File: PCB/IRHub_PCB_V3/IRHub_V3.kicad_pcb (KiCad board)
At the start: 2 copper layers, 85 parts, among them Q1 UMH3N, SW1 SW_Push, U1 DRV2605LDGS

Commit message: power pcb done
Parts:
- 5V1, TP9, T_D+1, T_D-1, T_D6, T_D7, T_GND1, T_RX1, T_TX1: footprint TestPoint:TestPoint_Pad_D2.0mm -> TestPoint:TestPoint_Pad_D1.0mm
- moved TP9 173.7 mm to (174.5, 120.5), turned to 180 degrees
- moved T_GND1 154.7 mm to (154.2, 128.5), turned to 180 degrees
- moved 5V1 154.4 mm to (145.8, 128.5), turned to 180 degrees
- moved T_D-1 151.6 mm to (151.5, 128.5), turned to 180 degrees
- moved T_D+1 151.1 mm to (148.5, 128.5), turned to 180 degrees
- moved AMS1117 147.6 mm to (161.5, 121.2)
- moved D25 146.3 mm to (184.9, 112.1), turned to -109.1 degrees
- moved D26 145.6 mm to (181.7, 118.8), turned to -120.6 degrees
- moved CH340C1 145.4 mm to (150.1, 122.5), turned to 90 degrees
- moved T_RX1 144.9 mm to (160.8, 98.0)
- moved ESP1 144.6 mm to (150.0, 99.5)
- moved C4 144.3 mm to (168.5, 124.8)
- moved D27 143.6 mm to (177.3, 124.8), turned to -132.1 degrees
- moved D1 143.0 mm to (141.5, 136.0), turned to 166.9 degrees
- moved T_TX1 142.8 mm to (160.8, 95.8), turned to 180 degrees
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
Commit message: finished placement
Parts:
- removed ME6211: ME6211C33M5, Package_TO_SOT_SMD:SOT-23-5
- moved R10 158.4 mm to (178.2, 116.1), turned to -22.5 degrees
- moved R9 152.9 mm to (181.3, 91.3), turned to 22.5 degrees
- moved MFT1 152.3 mm to (170.7, 100.7)
- moved R11 147.6 mm to (158.5, 131.2), turned to -67.5 degrees
- moved BZR1 141.6 mm to (178.4, 100.8), turned to -90 degrees
- moved R16 137.3 mm to (162.3, 108.8)
- moved R15 136.2 mm to (162.2, 103.2), turned to 180 degrees
- moved R12 135.6 mm to (133.9, 128.2), turned to -112.5 degrees
- moved R8 133.6 mm to (166.1, 71.8), turned to 67.5 degrees
- moved R18 132.9 mm to (162.3, 106.0)
- moved R5 132.7 mm to (134.2, 118.0), turned to -90 degrees
- moved MFT2 122.3 mm to (130.1, 118.0), turned to 180 degrees
- moved R6 122.1 mm to (137.7, 100.0)
- moved DispTouch1 120.0 mm to (169.4, 81.8), turned to 90 degrees
- moved LRA1 118.6 mm to (130.5, 92.0), turned to -90 degrees
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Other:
- board outline added: 80 x 80 mm

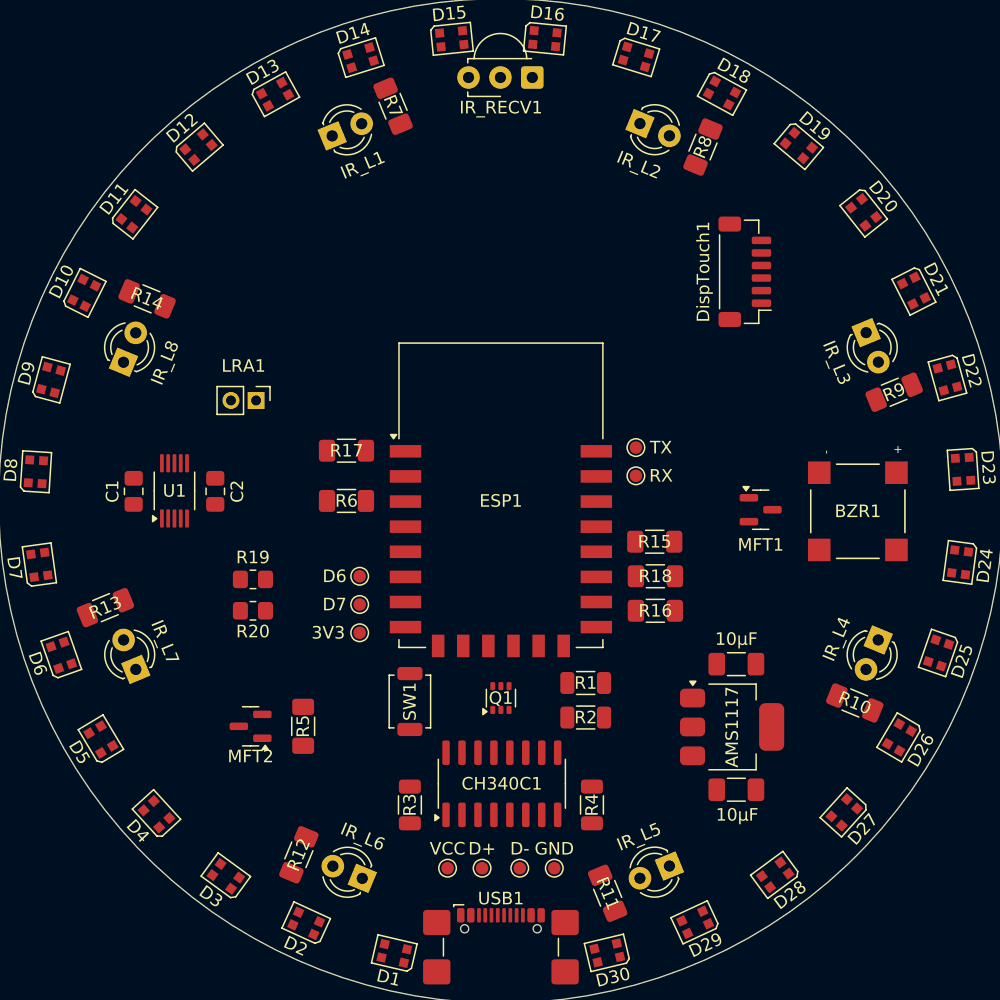
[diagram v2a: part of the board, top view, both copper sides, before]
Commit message: update resistor values
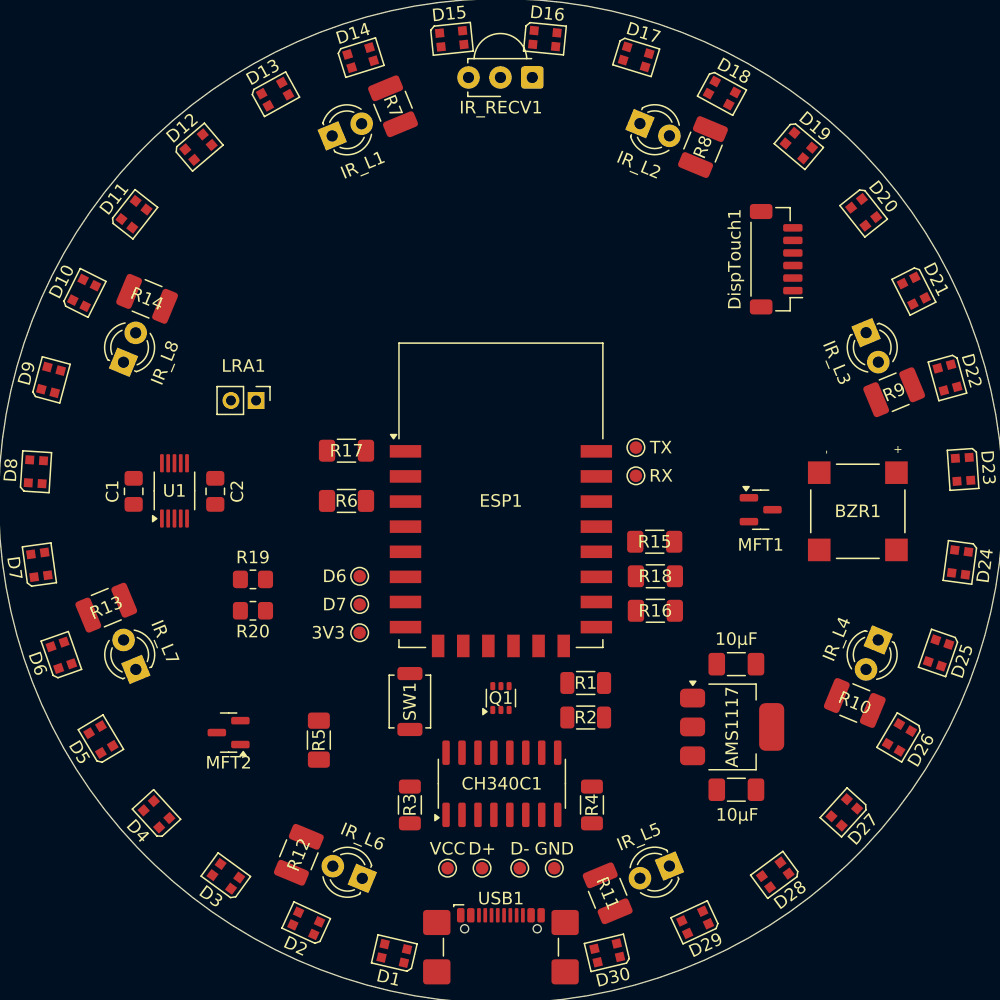
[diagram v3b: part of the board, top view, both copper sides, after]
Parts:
- R10, R11, R12, R13, R14, R7, R8, R9: value 68 -> 43; footprint Resistor_SMD:R_1206_3216Metric_Pad1.30x1.75mm_HandSolder -> Resistor_SMD:R_1210_3225Metric_Pad1.30x2.65mm_HandSolder
- moved DispTouch1 2.69 mm to (171.9, 80.8)
- moved MFT2 1.82 mm to (128.3, 118.5)
- moved R5 1.67 mm to (135.5, 119.0)
- moved R13 0.07 mm to (118.6, 108.5)

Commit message: complete pcb design
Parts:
- moved C2 4.65 mm to (122.6, 99.0)
- moved C1 4.20 mm to (125.0, 99.0)
- moved U1 4.20 mm to (128.2, 99.0)
- moved R2 2.85 mm to (156.9, 114.4)
- moved R20 2.73 mm to (129.8, 106.0)
- moved R1 2.60 mm to (156.8, 117.1)
- moved R19 2.33 mm to (129.8, 108.5)
- moved R9 0.13 mm to (181.4, 91.4)
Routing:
- net +5V: track 0.00 -> 292.0 mm, vias 0 -> 4
- net IR_GND: track 0.00 -> 236.8 mm
- net +3.3V: track 0.00 -> 207.0 mm, vias 0 -> 1
- net D1: track 0.00 -> 82.4 mm, vias 0 -> 4
- net D2: track 0.00 -> 71.6 mm, vias 0 -> 4
- net D5: track 0.00 -> 53.9 mm
- net D0: track 0.00 -> 48.5 mm, vias 0 -> 2
- net D7: track 0.00 -> 48.1 mm, vias 0 -> 4
- net GND: track 0.00 -> 39.1 mm, vias 0 -> 95
- net RST: track 0.00 -> 34.4 mm
- net TX: track 0.00 -> 30.1 mm
- net RX: track 0.00 -> 24.0 mm
- net D3: track 0.00 -> 20.7 mm
- net D6: track 0.00 -> 17.4 mm, vias 0 -> 2
- net Net-(CH340C1-TXD): track 0.00 -> 15.2 mm, vias 0 -> 2
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- added copper zone on B.Cu, net GND
- added copper zone on F.Cu, net GND

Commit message: final board design i hope
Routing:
- net GND: track 39.1 -> 41.2 mm, vias 95 -> 110
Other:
- board text added: "15th September 2025"
- board text added: "IR Hub Rev. 3 Madhukar Temba"

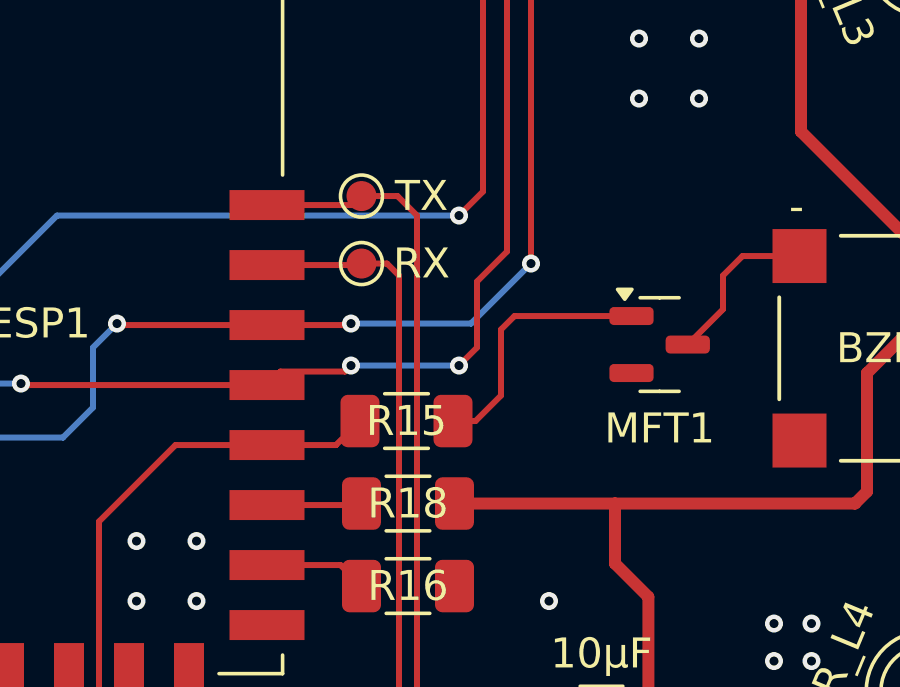
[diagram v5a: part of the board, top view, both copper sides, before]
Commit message: added one missing res 👀
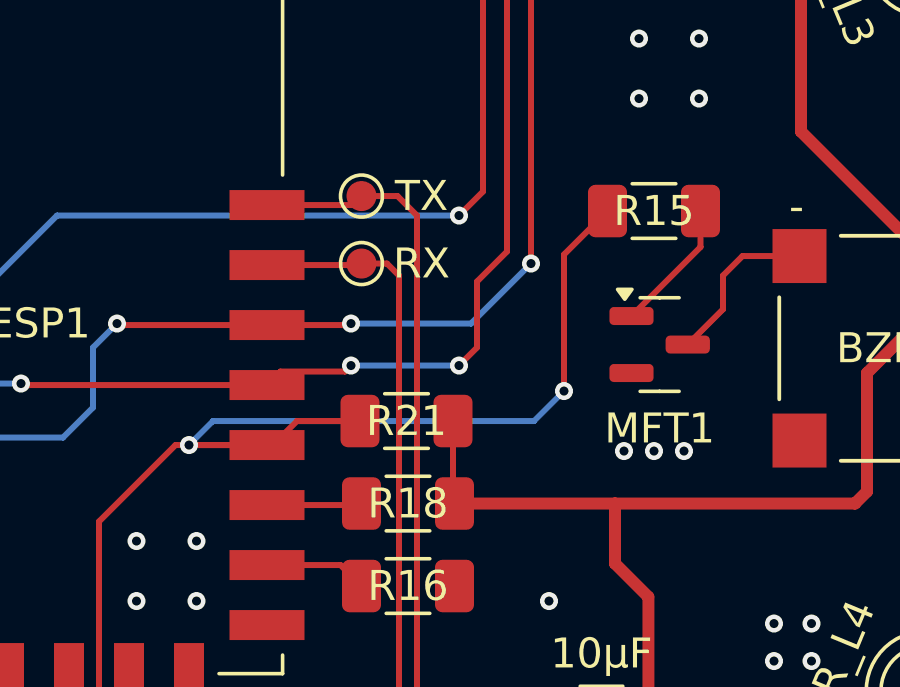
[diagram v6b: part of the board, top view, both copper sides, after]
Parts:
- added R21: 12000, Resistor_SMD:R_1206_3216Metric_Pad1.30x1.75mm_HandSolder, F.Cu at (162.2, 103.2)
- moved R15 10.8 mm to (170.5, 96.2)
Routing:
- net D3: track 20.7 -> 43.1 mm, vias 0 -> 2
- net Net-(MFT1-G): track 8.69 -> 4.45 mm
- net +3.3V: track 207.0 -> 209.8 mm
- net GND: vias 110 -> 113
